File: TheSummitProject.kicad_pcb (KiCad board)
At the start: 4 copper layers, 70 x 65 mm, 81 parts, among them IC1 STM32U5F7VJT6, J1 Cortex SWD, J4 Screen FPC, J5 Micro_SD_Card_Det1, Q1 NMOS, SW1 SW_SPDT, SW2 PWR_BTN, U1 NPM1300-CAAA-R, U2 USBLC6-2SC6, U3 USBLC6-2SC6, Y1 16Mhz, Y2 32.768Khz

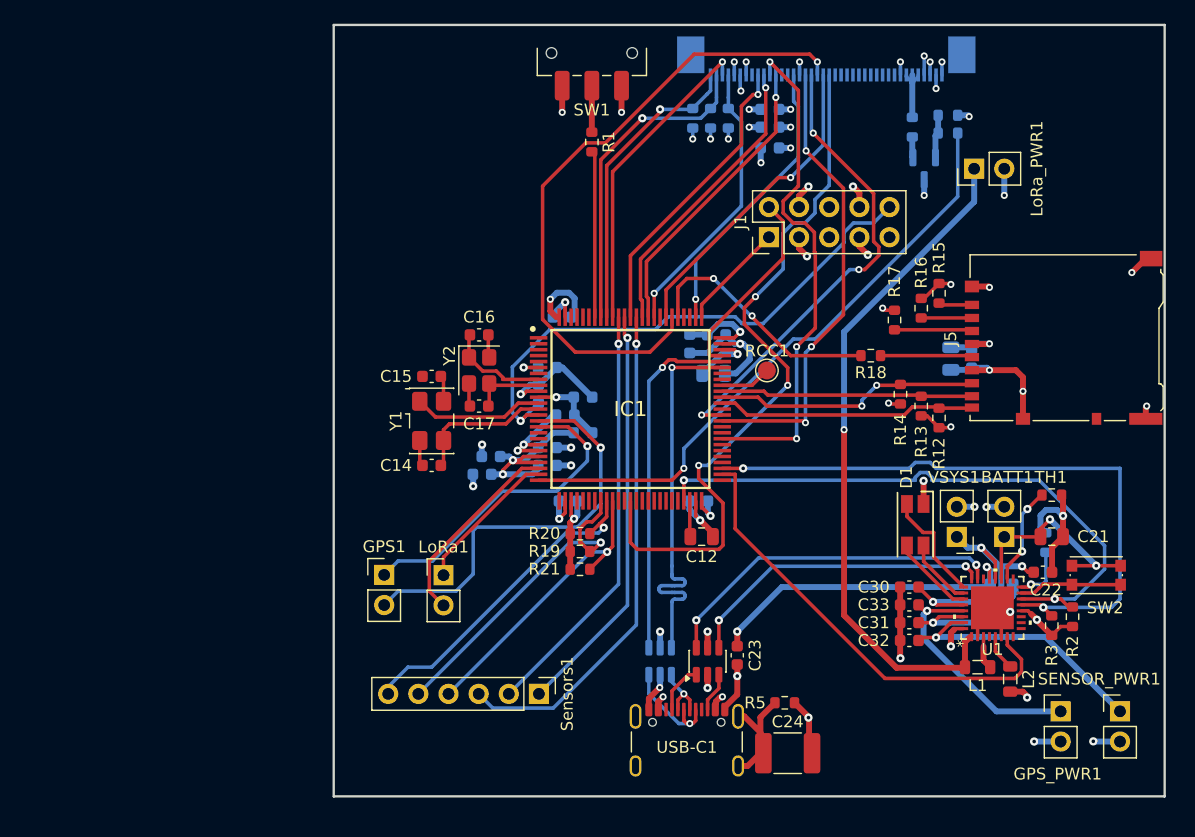
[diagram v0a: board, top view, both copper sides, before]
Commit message: Redesigned PCB layout 90% done
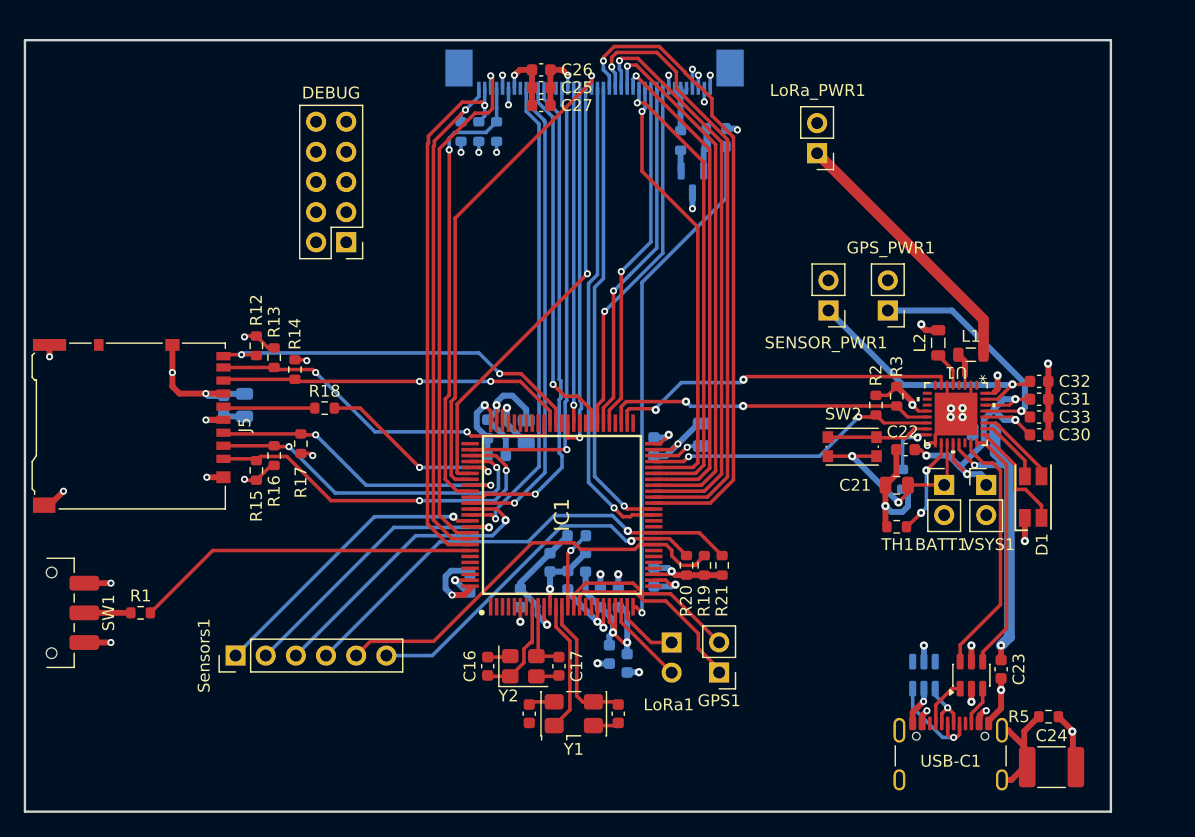
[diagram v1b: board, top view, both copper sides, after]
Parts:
- removed RCC1: RCC, TestPoint:TestPoint_Pad_D1.5mm
- C12, LoRa1: moved to B.Cu
- C25, C26, C27: moved to F.Cu
- moved J5 78.9 mm to (108.0, 101.9), turned to -90 degrees
- moved SW1 65.6 mm to (101.2, 117.7), turned to -90 degrees
- moved C29 63.1 mm to (115.7, 100.2), turned to -90 degrees
- moved C28 59.6 mm to (117.5, 100.2), turned to -90 degrees
- moved R15 59.4 mm to (118.5, 105.7), turned to -90 degrees
- moved R12 57.8 mm to (118.5, 95.2), turned to -90 degrees
- moved R16 55.9 mm to (120.0, 104.4), turned to -90 degrees
- moved R1 54.9 mm to (108.7, 117.7), turned to 0 degrees
- moved R13 54.7 mm to (120.0, 96.2), turned to -90 degrees
- moved R17 51.1 mm to (122.2, 103.4), turned to -90 degrees
- moved R14 51.1 mm to (121.7, 97.2), turned to -90 degrees
- moved R18 46.2 mm to (124.2, 100.4), turned to 0 degrees
- moved SENSOR_PWR1 41.8 mm to (166.7, 92.2), turned to 180 degrees
- moved GPS_PWR1 36.8 mm to (171.7, 92.2), turned to 180 degrees
- moved DEBUG 35.6 mm to (126.1, 86.5), turned to 180 degrees
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- renumbered J1 to DEBUG
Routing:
- net LCD_D6: track 0.00 -> 54.6 mm, vias 0 -> 1
- net LCD_D7: track 0.00 -> 51.9 mm, vias 0 -> 1
- net LCD_D8: track 0.00 -> 48.3 mm, vias 0 -> 1
- net LCD_D9: track 0.00 -> 45.4 mm, vias 0 -> 1
- net LCD_D10: track 0.00 -> 41.9 mm, vias 0 -> 1
- net /MCU/NRST: track 47.0 -> 6.63 mm
- net LCD_D5: track 0.00 -> 39.1 mm, vias 0 -> 1
- net LCD_D11: track 0.00 -> 39.0 mm, vias 0 -> 1
- net LCD_D12: track 0.00 -> 37.6 mm, vias 0 -> 1
- net Net-(IC1-USB_OTG_HS_DM): track 33.6 -> 0.07 mm, vias 1 -> 0
- net +3.3V_DP_LORA: track 67.7 -> 35.0 mm, vias 11 -> 7
- net LCD_D15: track 0.00 -> 30.5 mm, vias 0 -> 1
- net LCD_D14: track 0.00 -> 30.1 mm, vias 0 -> 1
- net LCD_D13: track 0.00 -> 29.7 mm, vias 0 -> 1
- net Net-(IC1-USB_OTG_HS_DP): track 29.5 -> 0.00 mm, vias 1 -> 0
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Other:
- board size 70 x 65 mm -> 91.5 x 65 mm

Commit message: Layout PCB
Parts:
- added RCC1: RCC, TestPoint:TestPoint_Pad_D1.5mm, B.Cu at (140.5, 94.0)
- renumbered DEBUG to J1
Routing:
- net /MCU/NRST: track 6.63 -> 57.8 mm, vias 1 -> 3
- net Net-(IC1-USB_OTG_HS_DM): track 0.07 -> 47.4 mm, vias 0 -> 1
- net Net-(IC1-USB_OTG_HS_DP): track 0.00 -> 47.1 mm, vias 0 -> 1
- net Net-(IC1-DEBUG_JTMS-SWDIO): track 0.00 -> 25.4 mm, vias 0 -> 1
- net Net-(IC1-DEBUG_JTCK-SWCLK): track 0.00 -> 25.1 mm, vias 0 -> 1
- net Net-(USB-C1-SHIELD): track 9.52 -> 28.5 mm
- net LCD_PWM: track 43.2 -> 61.8 mm
- net GND: track 127.4 -> 140.3 mm, vias 35 -> 39
- net RCC_MCO: track 0.00 -> 9.16 mm, vias 0 -> 1
- net VSYS: track 29.7 -> 38.1 mm, vias 4 -> 5
- net LCD_D2: track 38.1 -> 41.3 mm
- net LCD_RST: track 38.9 -> 41.7 mm
- net +3.3V_DP_LORA: track 35.0 -> 37.8 mm
- net +3.3V: track 63.3 -> 65.8 mm, vias 17 -> 16
- net Net-(IC1-HSE_IN): track 11.0 -> 13.2 mm
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
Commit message: DFM tested and edited
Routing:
- net GND: track 140.3 -> 137.9 mm
- net +3.3V: track 65.8 -> 64.4 mm
- net Net-(USB-C1-SHIELD): track 28.5 -> 27.5 mm
- net Net-(IC1-HSE_OUT): track 12.1 -> 11.5 mm

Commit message: DFM tested and edited
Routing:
- net GND: track 137.9 -> 138.9 mm
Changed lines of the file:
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@@
 		(sheetname "/MCU/")
 		(sheetfile "TheSummitProject.kicad_sch")
-		(units
-			(unit
-				(name "A")
-				(pins "SH" "A1" "A12" "B1" "B12" "A4" "A9" "B4" "B9" "A5" "B5" "A7" "B7"
-					"A6" "B6"
-				)
-			)
-		)
 		(attr smd)
 		(duplicate_pad_numbers_are_jumpers no)
@@
 			(roundrect_rratio 0.25)
 		)
-		(pad "A9" smd roundrect
-			(at 2.4 -3.68)
-			(size 0.6 1.15)
-			(layers "F.Cu" "F.Mask" "F.Paste")
-			(roundrect_rratio 0.25)
-			(net "VBUS")
-			(pinfunction "VBUS_A9")
-			(pintype "passive")
-		)
-		(pad "A12" smd roundrect
-			(at 3.2 -3.68)
-			(size 0.6 1.15)
-			(layers "F.Cu" "F.Mask" "F.Paste")
-			(roundrect_rratio 0.25)
-			(net "GND")
-			(pinfunction "GND_A12")
-			(pintype "passive")
-		)
 		(pad "B1" smd roundrect
 			(at 3.2 -3.68)
@@
 			(roundrect_rratio 0.25)
 		)
-		(pad "B9" smd roundrect
-			(at -2.4 -3.68)
-			(size 0.6 1.15)
-			(layers "F.Cu" "F.Mask" "F.Paste")
-			(roundrect_rratio 0.25)
-			(net "VBUS")
-			(pinfunction "VBUS_B9")
-			(pintype "passive")
-		)
-		(pad "B12" smd roundrect
-			(at -3.2 -3.68)
-			(size 0.6 1.15)
-			(layers "F.Cu" "F.Mask" "F.Paste")
-			(roundrect_rratio 0.25)
-			(net "GND")
-			(pinfunction "GND_B12")
-			(pintype "passive")
-		)
 		(pad "SH" thru_hole oval
 			(at -4.32 -3.105)
@@
 		(tags "resistor")
 		(property "Reference" "R5"
-			(at 2.5 0 0)
+			(at -0.019239 1.421934 0)
 			(layer "F.SilkS")
 			(effects
@@
 		(tags "NPM1300-QEAA-R7 ")
 		(property "Reference" "U1"
-			(at -3.5 0 180)
+			(at -3.671934 0 180)
 			(unlocked yes)
 			(layer "F.SilkS")
@@
 		)
 		(fp_text user "*"
-			(at -3 -2.5 90)
+			(at -3.171934 -2.564214 90)
 			(layer "F.SilkS")
 			(effects
@@
 		(sheetname "/SD/")
 		(sheetfile "sd.kicad_sch")
-		(units
-			(unit
-				(name "A")
-				(pins "1" "2" "3" "4" "5" "6" "7" "8" "9" "SH")
-			)
-		)
 		(attr smd)
 		(duplicate_pad_numbers_are_jumpers no)
@@
 		(fp_line
 			(start -5.945 8.385)
-			(end -6.145 8.185)
+			(end -6.045 8.285)
 			(stroke
 				(width 0.12)
@@
 	)
 	(segment
+		(start 175.758786 103.274635)
+		(end 175.758786 102.491214)
+		(width 0.2)
+		(layer "F.Cu")
+		(net "GND")
+	)
+	(segment
 		(start 175.685787 103.347634)
 		(end 175.239651 103.347634)
@@
 	)
 	(segment
-		(start 176.685785 100.126958)
-		(end 176.685785 98.496234)
-		(width 0.254)
-		(layer "F.Cu")
-		(net "GND")
-	)
-	(segment
 		(start 153.349624 115.296929)
 		(end 153.796531 115.296929)
@@
 	)
 	(segment
+		(start 175.685787 103.347634)
+		(end 175.758786 103.274635)
+		(width 0.2)
+		(layer "F.Cu")
+		(net "GND")
+	)
+	(segment
 		(start 147.224629 118.275371)
 		(end 146.9 118.6)
@@
 	)
 	(segment
+		(start 175.758786 102.491214)
+		(end 177 101.25)
+		(width 0.2)
+		(layer "F.Cu")
+		(net "GND")
+	)
+	(segment
 		(start 141.474629 125.396934)
 		(end 143.349629 125.396934)
@@
 	)
 	(segment
-		(start 176.902695 101.25)
-		(end 175.731786 102.420909)
-		(width 0.254)
-		(layer "F.Cu")
-		(net "GND")
-	)
-	(segment
 		(start 146.874629 127.171934)
 		(end 148.749629 127.171934)
@@
 	)
 	(segment
-		(start 175.731786 102.420909)
-		(end 175.731786 103.301635)
-		(width 0.254)
-		(layer "F.Cu")
-		(net "GND")
-	)
-	(segment
-		(start 178.685786 99.716909)
-		(end 178.685786 98.496234)
-		(width 0.254)
+		(start 115.705761 106.246934)
+		(end 114.305761 106.246934)
+		(width 0.5)
 		(layer "F.Cu")
 		(net "GND")
 	)
 	(segment
-		(start 115.705761 106.246934)
-		(end 114.305761 106.246934)
-		(width 0.5)
+		(start 176.685785 99.935785)
+		(end 177 100.25)
+		(width 0.2)
 		(layer "F.Cu")
 		(net "GND")
@@
 	)
 	(segment
+		(start 176.685785 98.496234)
+		(end 176.685785 99.935785)
+		(width 0.2)
+		(layer "F.Cu")
+		(net "GND")
+	)
+	(segment
 		(start 153.958827 103.443868)
 		(end 153.480761 103.921934)
@@
 	)
 	(segment
+		(start 178.685786 99.814214)
+		(end 178.25 100.25)
+		(width 0.2)
+		(layer "F.Cu")
+		(net "GND")
+	)
+	(segment
 		(start 139.9 125.396934)
 		(end 141.474629 125.396934)
@@
 		(layer "F.Cu")
 		(net "GND")
+	)
+	(segment
+		(start 178.685786 98.496234)
+		(end 178.685786 99.814214)
+		(width 0.2)
+		(layer "F.Cu")
+		(net "GND")
